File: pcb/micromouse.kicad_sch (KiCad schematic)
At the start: 24 parts, among them J1 AVR-ISP-6, J2 Conn_01x02, J4 Conn_01x02, Q1 Si2319CDS, U1 TSSP77038ETR, U2 TSSP77038ETR, U3 TSSP77038ETR, U4 TSSP77038ETR, U5 TSSP77038ETR, U6 TSSP77038ETR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

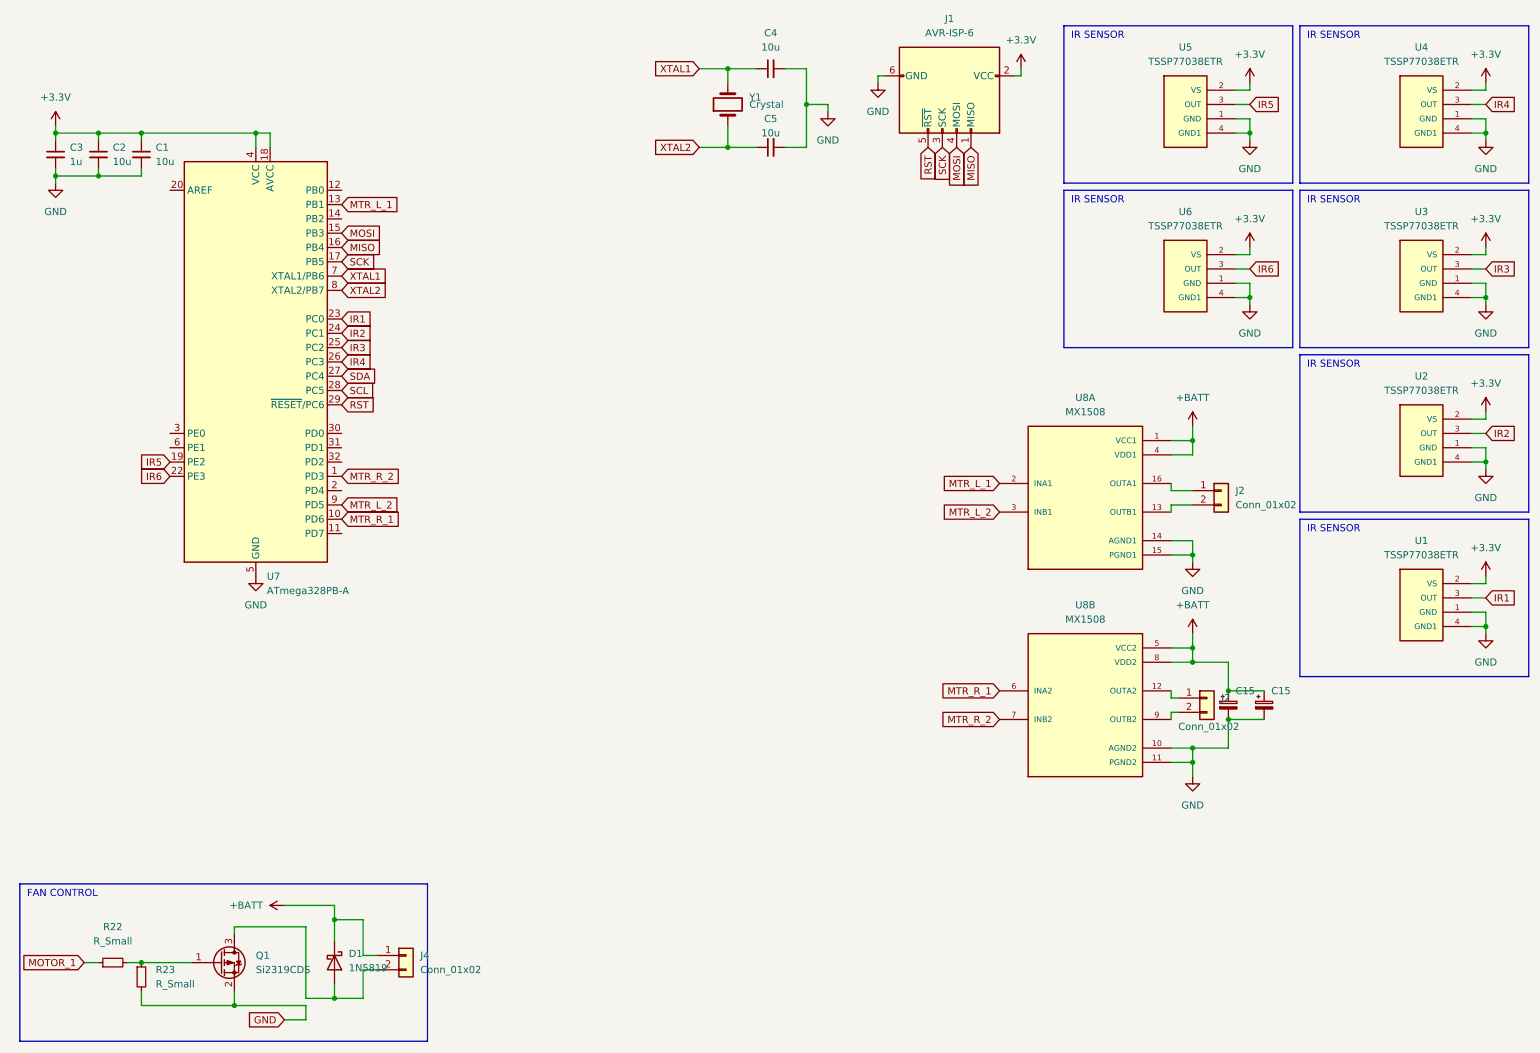
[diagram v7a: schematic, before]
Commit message: add IR 3d + pin i2c screen
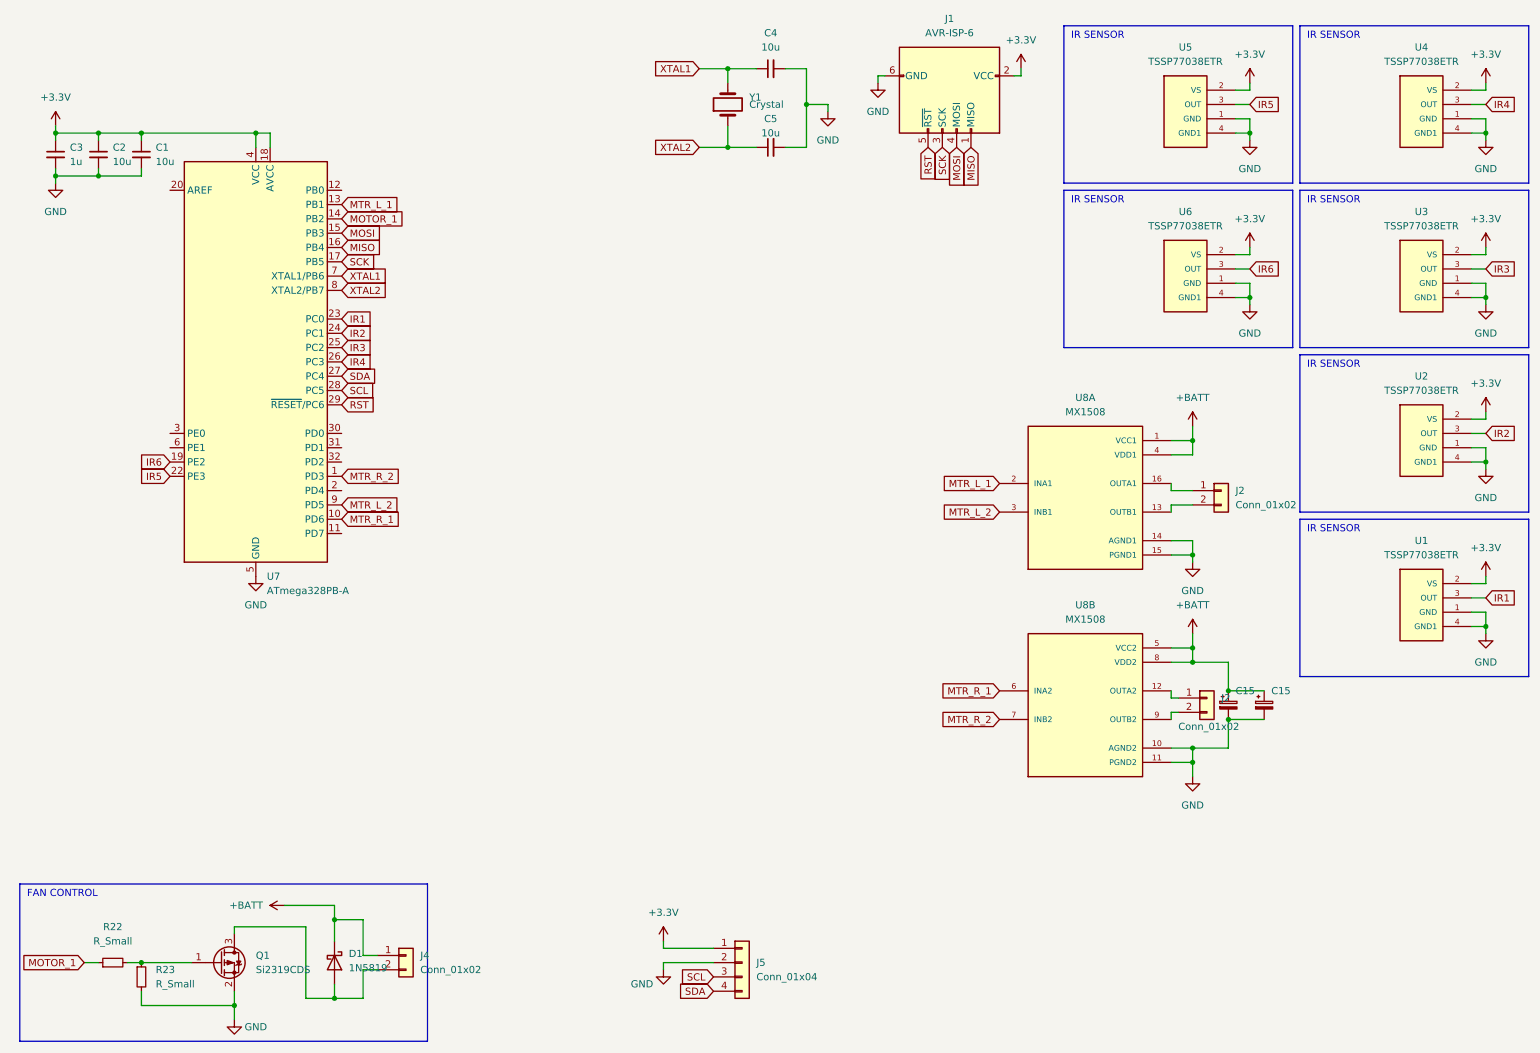
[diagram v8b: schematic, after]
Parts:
- added J5: Conn_01x04, Connector_PinHeader_2.54mm:PinHeader_1x04_P2.54mm_Vertical, symbol Connector_Generic:Conn_01x04
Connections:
- net +3.3V: now also J5.1 (Pin_1)
- net GND: now also J5.2 (Pin_2)
- net IR5: now also U7.22 (PE3); no longer U7.19 (PE2)
- net IR6: now also U7.19 (PE2); no longer U7.22 (PE3)
- net MOTOR_1: now also U7.14 (PB2)
- net SCL: now also J5.3 (Pin_3)
- net SDA: now also J5.4 (Pin_4)
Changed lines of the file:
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@@
-    (stroke (width 0) (type default))
-  )
-  (wire (pts (xy 60.96 191.77) (xy 64.77 191.77))
     (stroke (width 0) (type default))
   )
@@
     (stroke (width 0) (type default))
   )
-  (wire (pts (xy 52.07 189.23) (xy 64.77 189.23))
-    (stroke (width 0) (type default))
-  )
   (wire (pts (xy 271.78 55.88) (xy 274.32 55.88))
     (stroke (width 0) (type default))
@@
     (stroke (width 0) (type default))
   )
+  (wire (pts (xy 128.27 177.8) (xy 128.27 179.07))
+    (stroke (width 0) (type default))
+  )
   (wire (pts (xy 219.71 137.16) (xy 218.44 137.16))
     (stroke (width 0) (type default))
@@
     (stroke (width 0) (type default))
   )
+  (wire (pts (xy 128.27 182.88) (xy 128.27 181.61))
+    (stroke (width 0) (type default))
+  )
   (wire (pts (xy 229.87 26.67) (xy 232.41 26.67))
     (stroke (width 0) (type default))
@@
     (stroke (width 0) (type default))
   )
+  (wire (pts (xy 128.27 181.61) (xy 137.16 181.61))
+    (stroke (width 0) (type default))
+  )
   (wire (pts (xy 228.6 128.27) (xy 228.6 133.35))
     (stroke (width 0) (type default))
@@
     (stroke (width 0) (type default))
   )
-  (wire (pts (xy 64.77 189.23) (xy 64.77 191.77))
+  (wire (pts (xy 52.07 189.23) (xy 52.07 191.77))
     (stroke (width 0) (type default))
   )
@@
   )
   (wire (pts (xy 134.62 22.86) (xy 139.7 22.86))
+    (stroke (width 0) (type default))
+  )
+  (wire (pts (xy 137.16 179.07) (xy 128.27 179.07))
     (stroke (width 0) (type default))
   )
@@
     (property "Intersheetrefs" "${INTERSHEET_REFS}" (at 77.1101 67.31 0)
       (effects (font (size 1.27 1.27)) (justify left) hide)
+    )
+  )
+  (global_label "SDA" (shape input) (at 137.16 186.69 180) (fields_autoplaced)
+    (effects (font (size 1.27 1.27)) (justify right))
+    (property "Intersheetrefs" "${INTERSHEET_REFS}" (at 130.6861 186.69 0)
+      (effects (font (size 1.27 1.27)) (justify right) hide)
+    )
+  )
+  (global_label "IR6" (shape input) (at 40.64 92.71 180) (fields_autoplaced)
+    (effects (font (size 1.27 1.27)) (justify right))
+    (property "Intersheetrefs" "${INTERSHEET_REFS}" (at 34.6499 92.71 0)
+      (effects (font (size 1.27 1.27)) (justify right) hide)
     )
   )
@@
     )
   )
-  (global_label "GND" (shape input) (at 60.96 191.77 180) (fields_autoplaced)
-    (effects (font (size 1.27 1.27)) (justify right))
-    (property "Intersheetrefs" "${INTERSHEET_REFS}" (at 54.6764 191.6906 0)
-      (effects (font (size 1.27 1.27)) (justify right) hide)
-    )
-  )
   (global_label "MOSI" (shape input) (at 180.34 36.83 270) (fields_autoplaced)
     (effects (font (size 1.27 1.27)) (justify right))
@@
     )
   )
-  (global_label "IR6" (shape input) (at 40.64 95.25 180) (fields_autoplaced)
+  (global_label "SDA" (shape input) (at 71.12 77.47 0) (fields_autoplaced)
+    (effects (font (size 1.27 1.27)) (justify left))
+    (property "Intersheetrefs" "${INTERSHEET_REFS}" (at 77.5939 77.47 0)
+      (effects (font (size 1.27 1.27)) (justify left) hide)
+    )
+  )
+  (global_label "IR1" (shape input) (at 274.32 116.84 0) (fields_autoplaced)
+    (effects (font (size 1.27 1.27)) (justify left))
+    (property "Intersheetrefs" "${INTERSHEET_REFS}" (at 280.3101 116.84 0)
+      (effects (font (size 1.27 1.27)) (justify left) hide)
+    )
+  )
+  (global_label "XTAL2" (shape input) (at 71.12 62.23 0) (fields_autoplaced)
+    (effects (font (size 1.27 1.27)) (justify left))
+    (property "Intersheetrefs" "${INTERSHEET_REFS}" (at 79.5291 62.23 0)
+      (effects (font (size 1.27 1.27)) (justify left) hide)
+    )
+  )
+  (global_label "MTR_R_1" (shape input) (at 71.12 102.87 0) (fields_autoplaced)
+    (effects (font (size 1.27 1.27)) (justify left))
+    (property "Intersheetrefs" "${INTERSHEET_REFS}" (at 82.1295 102.87 0)
+      (effects (font (size 1.27 1.27)) (justify left) hide)
+    )
+  )
+  (global_label "SCL" (shape input) (at 137.16 184.15 180) (fields_autoplaced)
     (effects (font (size 1.27 1.27)) (justify right))
-    (property "Intersheetrefs" "${INTERSHEET_REFS}" (at 34.6499 95.25 0)
-      (effects (font (size 1.27 1.27)) (justify right) hide)
-    )
-  )
-  (global_label "SDA" (shape input) (at 71.12 77.47 0) (fields_autoplaced)
-    (effects (font (size 1.27 1.27)) (justify left))
-    (property "Intersheetrefs" "${INTERSHEET_REFS}" (at 77.5939 77.47 0)
-      (effects (font (size 1.27 1.27)) (justify left) hide)
-    )
-  )
-  (global_label "IR1" (shape input) (at 274.32 116.84 0) (fields_autoplaced)
-    (effects (font (size 1.27 1.27)) (justify left))
-    (property "Intersheetrefs" "${INTERSHEET_REFS}" (at 280.3101 116.84 0)
-      (effects (font (size 1.27 1.27)) (justify left) hide)
-    )
-  )
-  (global_label "XTAL2" (shape input) (at 71.12 62.23 0) (fields_autoplaced)
-    (effects (font (size 1.27 1.27)) (justify left))
-    (property "Intersheetrefs" "${INTERSHEET_REFS}" (at 79.5291 62.23 0)
-      (effects (font (size 1.27 1.27)) (justify left) hide)
-    )
-  )
-  (global_label "MTR_R_1" (shape input) (at 71.12 102.87 0) (fields_autoplaced)
-    (effects (font (size 1.27 1.27)) (justify left))
-    (property "Intersheetrefs" "${INTERSHEET_REFS}" (at 82.1295 102.87 0)
-      (effects (font (size 1.27 1.27)) (justify left) hide)
-    )
-  )
-  (global_label "IR5" (shape input) (at 40.64 92.71 180) (fields_autoplaced)
-    (effects (font (size 1.27 1.27)) (justify right))
-    (property "Intersheetrefs" "${INTERSHEET_REFS}" (at 34.6499 92.71 0)
+    (property "Intersheetrefs" "${INTERSHEET_REFS}" (at 130.7466 184.15 0)
       (effects (font (size 1.27 1.27)) (justify right) hide)
     )
@@
     )
   )
+  (global_label "IR5" (shape input) (at 40.64 95.25 180) (fields_autoplaced)
+    (effects (font (size 1.27 1.27)) (justify right))
+    (property "Intersheetrefs" "${INTERSHEET_REFS}" (at 34.6499 95.25 0)
+      (effects (font (size 1.27 1.27)) (justify right) hide)
+    )
+  )
   (global_label "MTR_L_2" (shape input) (at 187.96 101.6 180) (fields_autoplaced)
     (effects (font (size 1.27 1.27)) (justify right))
@@
     )
   )
+  (global_label "MOTOR_1" (shape input) (at 71.12 49.53 0) (fields_autoplaced)
+    (effects (font (size 1.27 1.27)) (justify left))
+    (property "Intersheetrefs" "${INTERSHEET_REFS}" (at 82.5529 49.53 0)
+      (effects (font (size 1.27 1.27)) (justify left) hide)
+    )
+  )
   (global_label "XTAL2" (shape input) (at 134.62 36.83 180) (fields_autoplaced)
     (effects (font (size 1.27 1.27)) (justify right))
@@
     )
   )
+  (symbol (lib_id "Connector_Generic:Conn_01x04") (at 142.24 181.61 0) (unit 1)
+    (in_bom yes) (on_board yes) (dnp no) (fields_autoplaced)
+    (property "Reference" "J5" (at 144.78 181.61 0)
+      (effects (font (size 1.27 1.27)) (justify left))
+    )
+    (property "Value" "Conn_01x04" (at 144.78 184.15 0)
+      (effects (font (size 1.27 1.27)) (justify left))
+    )
+    (property "Footprint" "Connector_PinHeader_2.54mm:PinHeader_1x04_P2.54mm_Vertical" (at 142.24 181.61 0)
+      (effects (font (size 1.27 1.27)) hide)
+    )
+    (property "Datasheet" "~" (at 142.24 181.61 0)
+      (effects (font (size 1.27 1.27)) hide)
+    )
+    (pin "1")
+    (pin "2")
+    (pin "3")
+    (pin "4")
+    (instances
+      (project "micromouse"
+        (path "/405a5ba7-3106-45d0-abc8-375c92cb441a"
+          (reference "J5") (unit 1)
+        )
+      )
+    )
+  )
   (symbol (lib_id "power:+BATT") (at 222.25 86.36 0) (unit 1)
     (in_bom yes) (on_board yes) (dnp no) (fields_autoplaced)
@@
         (path "/cb10bbf7-c2c1-4a0d-8947-ad707931d83b"
           (reference "C23") (unit 1)
+        )
+      )
+    )
+  )
+  (symbol (lib_id "power:+3.3V") (at 128.27 177.8 0) (unit 1)
+    (in_bom yes) (on_board yes) (dnp no) (fields_autoplaced)
+    (property "Reference" "#PWR024" (at 128.27 181.61 0)
+      (effects (font (size 1.27 1.27)) hide)
+    )
+    (property "Value" "+3.3V" (at 128.27 172.72 0)
+      (effects (font (size 1.27 1.27)))
+    )
+    (property "Footprint" "" (at 128.27 177.8 0)
+      (effects (font (size 1.27 1.27)) hide)
+    )
+    (property "Datasheet" "" (at 128.27 177.8 0)
+      (effects (font (size 1.27 1.27)) hide)
+    )
+    (pin "1")
+    (instances
+      (project "micromouse"
+        (path "/405a5ba7-3106-45d0-abc8-375c92cb441a"
+          (reference "#PWR024") (unit 1)
         )
       )
@@
     )
   )
+  (symbol (lib_id "power:GND") (at 128.27 182.88 0) (unit 1)
+    (in_bom yes) (on_board yes) (dnp no)
+    (property "Reference" "#PWR026" (at 128.27 189.23 0)
+      (effects (font (size 1.27 1.27)) hide)
+    )
+    (property "Value" "GND" (at 124.46 185.42 0)
+      (effects (font (size 1.27 1.27)))
+    )
+    (property "Footprint" "" (at 128.27 182.88 0)
+      (effects (font (size 1.27 1.27)) hide)
+    )
+    (property "Datasheet" "" (at 128.27 182.88 0)
+      (effects (font (size 1.27 1.27)) hide)
+    )
+    (pin "1")
+    (instances
+      (project "micromouse"
+        (path "/405a5ba7-3106-45d0-abc8-375c92cb441a"
+          (reference "#PWR026") (unit 1)
+        )
+      )
+    )
+  )
   (symbol (lib_id "Device:C_Small") (at 20.32 38.1 0) (unit 1)
     (in_bom yes) (on_board yes) (dnp no) (fields_autoplaced)
@@
         )
       )
+    )
+  )
+  (symbol (lib_id "power:GND") (at 52.07 191.77 0) (unit 1)
+    (in_bom yes) (on_board yes) (dnp no)
+    (property "Reference" "#PWR025" (at 52.07 198.12 0)
+      (effects (font (size 1.27 1.27)) hide)
+    )
+    (property "Value" "GND" (at 55.88 193.04 0)
+      (effects (font (size 1.27 1.27)))
+    )
+    (property "Footprint" "" (at 52.07 191.77 0)
+      (effects (font (size 1.27 1.27)) hide)
+    )
+    (property "Datasheet" "" (at 52.07 191.77 0)
+      (effects (font (size 1.27 1.27)) hide)
+    )
+    (pin "1")
+    (instances
+      (project "micromouse"
+        (path "/405a5ba7-3106-45d0-abc8-375c92cb441a"
+          (reference "#PWR025") (unit 1)
+        )
+      )
